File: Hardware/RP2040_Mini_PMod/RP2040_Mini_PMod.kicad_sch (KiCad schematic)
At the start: 37 parts, among them J3 Conn_02x06_Odd_Even, J4 USB_C_Receptacle_USB2.0, J5 Conn_01x04, SW1 SW_Push, SW2 SW_Push, U1 RP2040, U2 W25Q128JVS, U3 NCP1117-3.3_SOT223, Y1 12MHz

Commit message: continue with mini project
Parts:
- added J1: Micro_SD_Card, jjh:105162-0001, symbol Connector:Micro_SD_Card
- SW1, SW2: value SW_Push -> PTS815 SJK 250 SMTR LFS; footprint Button_Switch_THT:SW_PUSH_6mm_H4.3mm -> jjh:PTS815SJK250SMTRLFS
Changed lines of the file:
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@@
   (symbol (lib_id "Switch:SW_Push") (at 97.79 187.96 90) (unit 1)
     (in_bom yes) (on_board yes)
-    (property "Reference" "SW1" (id 0) (at 90.551 187.96 90))
-    (property "Value" "SW_Push" (id 1) (at 90.17 190.5 90))
-    (property "Footprint" "Button_Switch_THT:SW_PUSH_6mm_H4.3mm" (id 2) (at 92.71 187.96 0)
+    (property "Reference" "SW1" (id 0) (at 92.71 187.96 90))
+    (property "Value" "PTS815 SJK 250 SMTR LFS" (id 1) (at 87.63 180.34 0)
+      (effects (font (size 1.27 1.27)) hide)
+    )
+    (property "Footprint" "jjh:PTS815SJK250SMTRLFS" (id 2) (at 92.71 187.96 0)
       (effects (font (size 1.27 1.27)) hide)
     )
@@
   (symbol (lib_id "Switch:SW_Push") (at 144.78 182.88 90) (unit 1)
     (in_bom yes) (on_board yes)
-    (property "Reference" "SW2" (id 0) (at 137.541 182.88 0))
-    (property "Value" "SW_Push" (id 1) (at 139.8524 182.88 0))
-    (property "Footprint" "Button_Switch_THT:SW_PUSH_6mm_H4.3mm" (id 2) (at 139.7 182.88 0)
+    (property "Reference" "SW2" (id 0) (at 139.7 182.88 90))
+    (property "Value" "PTS815 SJK 250 SMTR LFS" (id 1) (at 139.8524 182.88 0)
+      (effects (font (size 1.27 1.27)) hide)
+    )
+    (property "Footprint" "jjh:PTS815SJK250SMTRLFS" (id 2) (at 139.7 182.88 0)
       (effects (font (size 1.27 1.27)) hide)
     )
@@
     (pin "1")
   )
+  (symbol (lib_id "Connector:Micro_SD_Card") (at 254 67.31 0) (unit 1)
+    (in_bom yes) (on_board yes) (fields_autoplaced)
+    (property "Reference" "J1" (id 0) (at 254.635 48.26 0))
+    (property "Value" "Micro_SD_Card" (id 1) (at 254.635 50.8 0))
+    (property "Footprint" "jjh:105162-0001" (id 2) (at 283.21 59.69 0)
+      (effects (font (size 1.27 1.27)) hide)
+    )
+    (property "Datasheet" "http://katalog.we-online.de/em/datasheet/693072010801.pdf" (id 3) (at 254 67.31 0)
+      (effects (font (size 1.27 1.27)) hide)
+    )
+    (pin "1")
+    (pin "2")
+    (pin "3")
+    (pin "4")
+    (pin "5")
+    (pin "6")
+    (pin "7")
+    (pin "8")
+    (pin "9")
+  )
   (symbol (lib_id "power:PWR_FLAG") (at 43.18 191.77 180) (unit 1)
     (in_bom yes) (on_board yes) (fields_autoplaced)
@@
       (reference "D3") (unit 1) (value "LED") (footprint "LED_SMD:LED_0603_1608Metric")
     )
+    (path "/e631d994-9bd2-4c7e-a12a-01901b43c7dc"
+      (reference "J1") (unit 1) (value "Micro_SD_Card") (footprint "jjh:105162-0001")
+    )
     (path "/00000000-0000-0000-0000-000060e95540"
       (reference "J3") (unit 1) (value "Conn_02x06_Odd_Even") (footprint "Connector_PinHeader_2.54mm:PinHeader_2x06_P2.54mm_Vertical")
@@
     )
     (path "/00000000-0000-0000-0000-000060ecf6f5"
-      (reference "SW1") (unit 1) (value "SW_Push") (footprint "Button_Switch_THT:SW_PUSH_6mm_H4.3mm")
+      (reference "SW1") (unit 1) (value "PTS815 SJK 250 SMTR LFS") (footprint "jjh:PTS815SJK250SMTRLFS")
     )
     (path "/00000000-0000-0000-0000-000060ed08d9"
-      (reference "SW2") (unit 1) (value "SW_Push") (footprint "Button_Switch_THT:SW_PUSH_6mm_H4.3mm")
+      (reference "SW2") (unit 1) (value "PTS815 SJK 250 SMTR LFS") (footprint "jjh:PTS815SJK250SMTRLFS")
     )
     (path "/00000000-0000-0000-0000-000060e8d0b0"

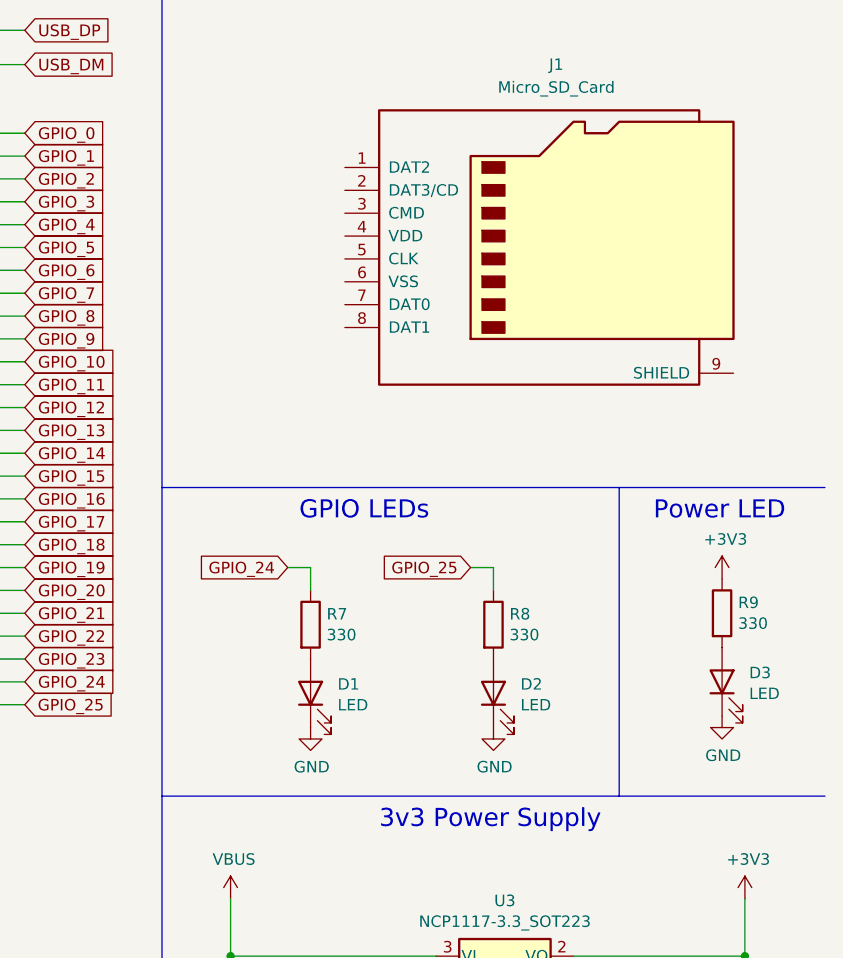
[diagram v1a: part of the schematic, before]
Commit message: Add the SD GPIO and RGB LED to schematic
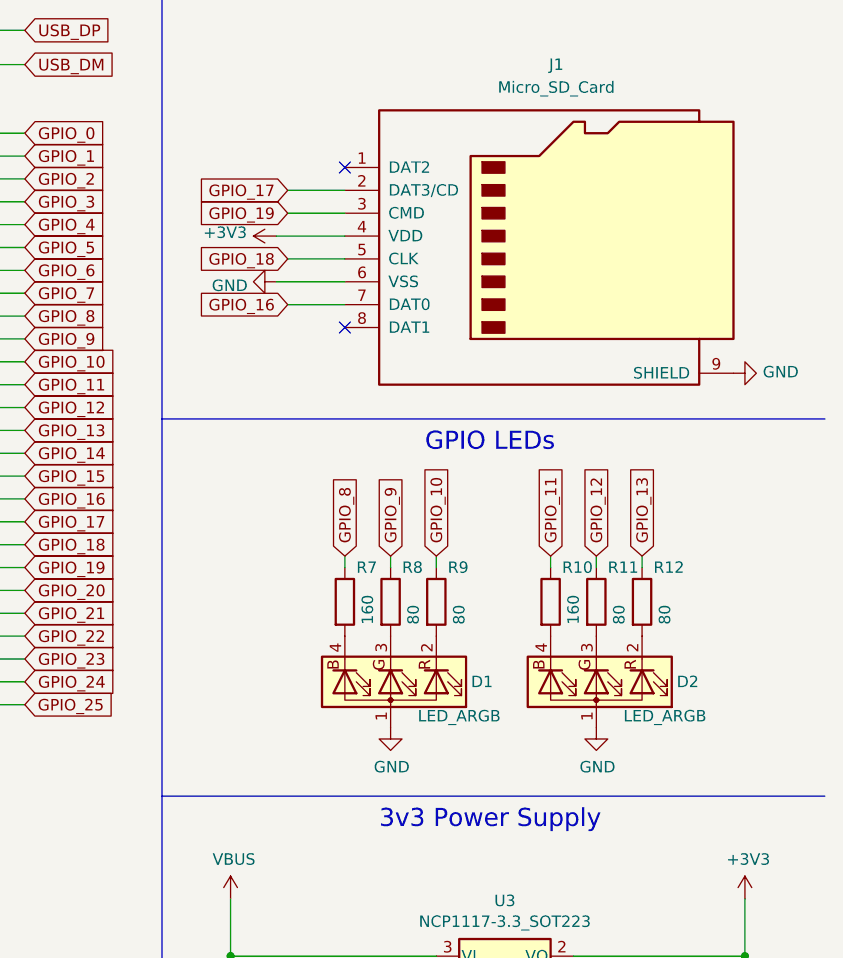
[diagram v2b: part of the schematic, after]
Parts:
- removed D1, D2, D3: LED, LED_SMD:LED_0603_1608Metric, symbol Device:LED
- added D1, D2: LED_ARGB, jjh:SX-0402-RGB, symbol Device:LED_ARGB
- added R10: 160, Resistor_SMD:R_0603_1608Metric, symbol Device:R
- added R11, R12: 80, Resistor_SMD:R_0603_1608Metric, symbol Device:R
- R7: value 330 -> 160
- R8, R9: value 330 -> 80
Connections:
- net +3V3: now also J1.4 (VDD); no longer R9.1
- net GND: now also J1.6 (VSS), J1.9 (SHIELD), D1.1 (A), D2.1 (A)
- net GPIO_10: now also R9.1
- net GPIO_11: now also R10.1
- net GPIO_12: now also R11.1
- net GPIO_13: now also R12.1
- net GPIO_16: now also J1.7 (DAT0)
- net GPIO_17: now also J1.2 (DAT3/CD)
- net GPIO_18: now also J1.5 (CLK)
- net GPIO_19: now also J1.3 (CMD)
- net GPIO_24: no longer R7.1
- net GPIO_25: no longer R8.1
- net GPIO_8: now also R7.1
- net GPIO_9: now also R8.1
- net at R7.2: now also D1.4 (BK)
- net at R8.2: now also D1.3 (GK)
- net at R9.2: now also D1.2 (RK)
- new net: D2.2 (RK), R12.2
- new net: D2.3 (GK), R11.2
- new net: D2.4 (BK), R10.2
- no-connect marks 6 -> 8
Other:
- note removed: "Power LED"

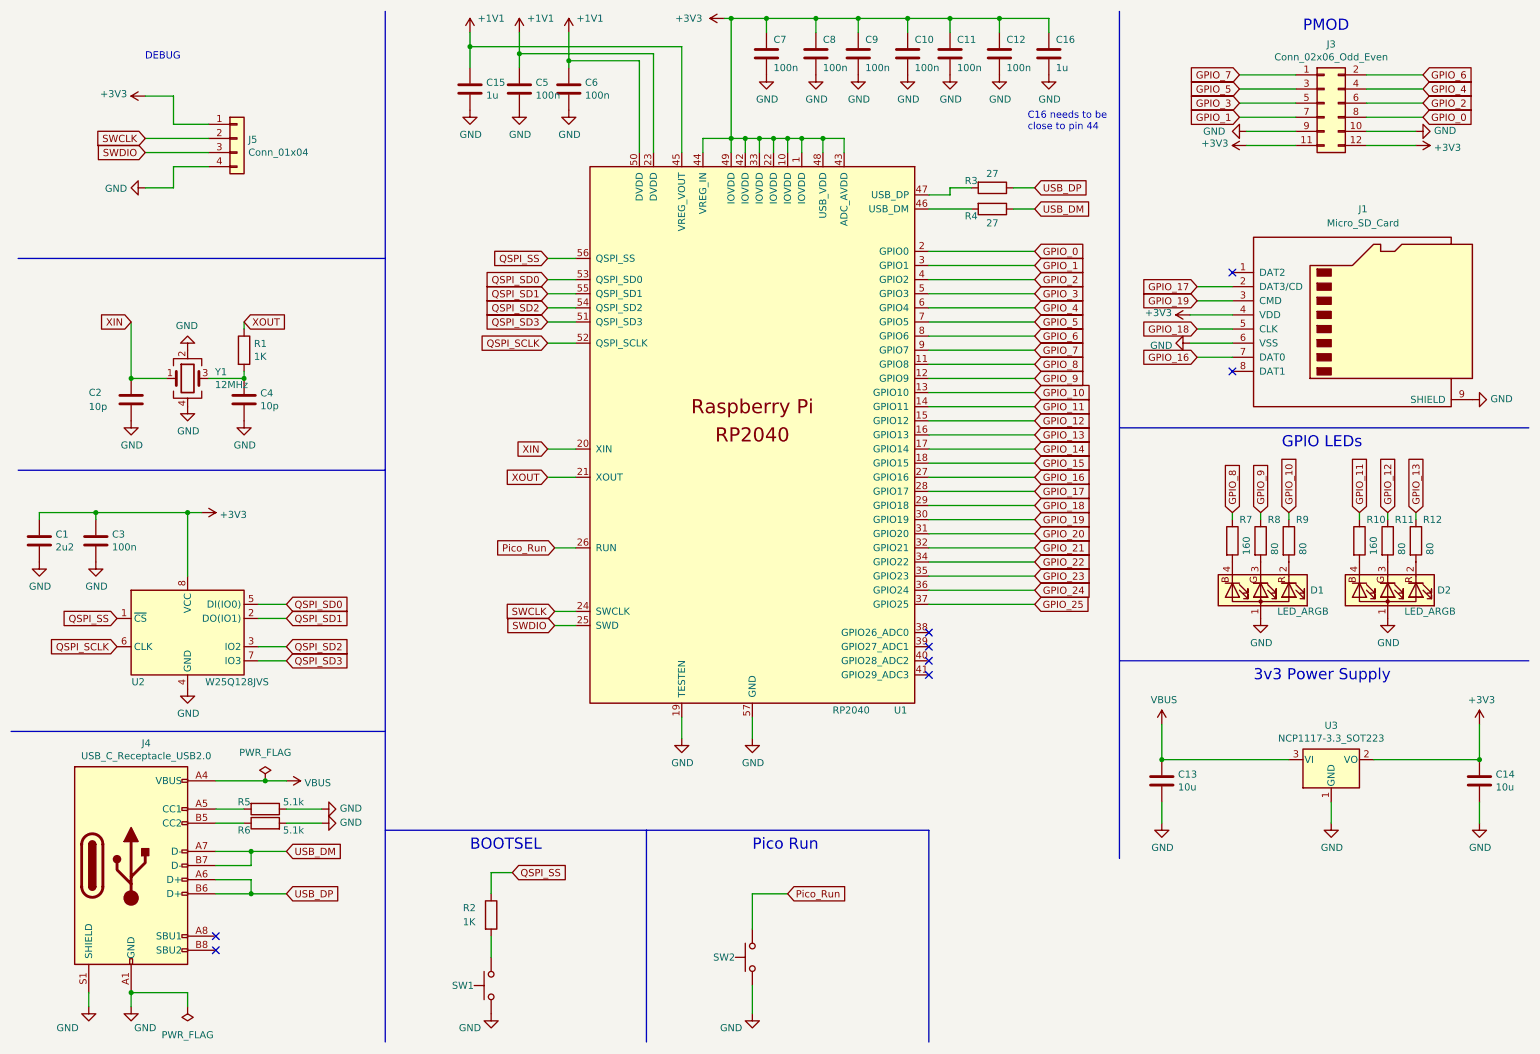
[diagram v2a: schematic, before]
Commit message: complete schematic and start pcb routing
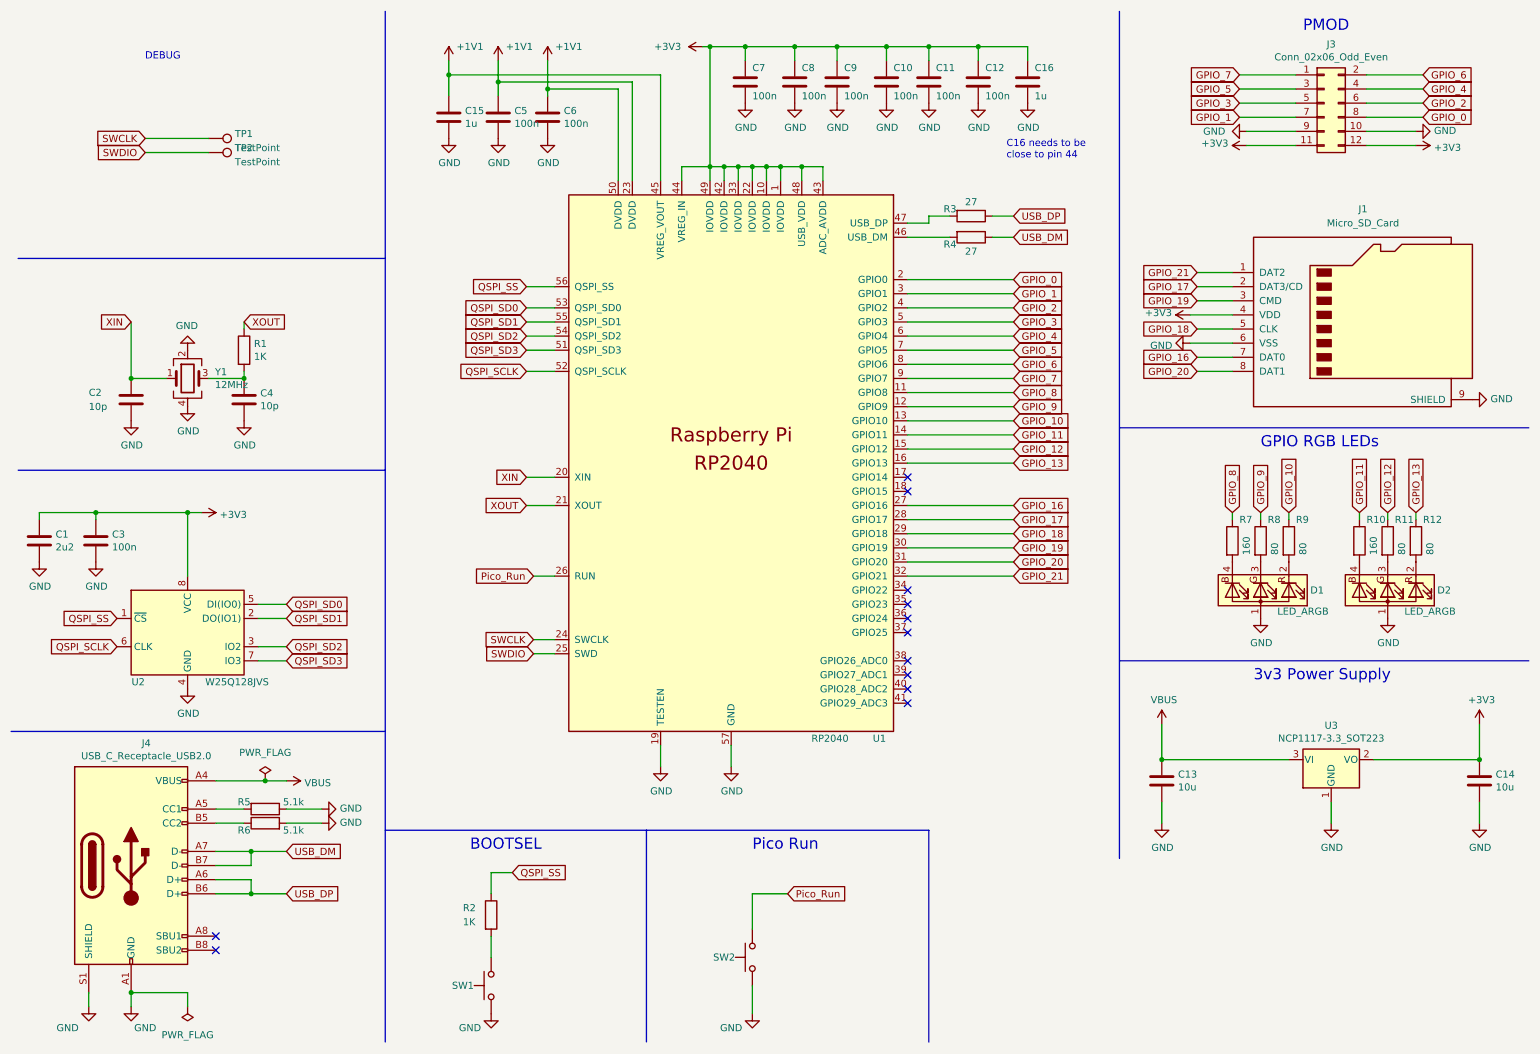
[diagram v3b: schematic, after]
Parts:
- removed J5: Conn_01x04, Connector_PinHeader_2.54mm:PinHeader_1x04_P2.54mm_Vertical, symbol Connector_Generic:Conn_01x04
- added TP1, TP2: TestPoint, TestPoint:TestPoint_Pad_D1.5mm, symbol Connector:TestPoint
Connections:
- net GPIO_20: now also J1.8 (DAT1)
- net GPIO_21: now also J1.1 (DAT2)
- net SWCLK: now also TP1.1
- net SWDIO: now also TP2.1
- net GPIO_14: no longer names the net of U1.17 (GPIO14)
- net GPIO_15: no longer names the net of U1.18 (GPIO15)
- net GPIO_22: no longer names the net of U1.34 (GPIO22)
- net GPIO_23: no longer names the net of U1.35 (GPIO23)
- net GPIO_24: no longer names the net of U1.36 (GPIO24)
- net GPIO_25: no longer names the net of U1.37 (GPIO25)
- no-connect marks 8 -> 12
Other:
- note added: "GPIO RGB LEDs"
- note removed: "GPIO LEDs"
- title: PMOD for Raspberry Pi RP2040 -> Mini PMOD RP2040
- moved on the sheet: C10, C11, C12, C15, C16, C5, C6, C7, C8, C9, R3, R4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

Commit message: update switch layout and sd card gnd pins
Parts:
- removed SW1, SW2: PTS815 SJK 250 SMTR LFS, jjh:PTS815SJK250SMTRLFS, symbol Switch:SW_Push
- added SW1, SW2: PTS815 SJK 250 SMTR LFS, jjh:PTS815SJK250SMTRLFS, symbol Switch:SW_MEC_5E
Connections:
- net GND: now also SW1.1, SW2.1
- net Pico_Run: now also SW1.4 (A)
- net at R2.2: now also SW2.4 (A)
- no-connect marks 12 -> 16
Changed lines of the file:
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@@
   (no_connect (at 172.72 124.46))
   (no_connect (at 172.72 137.16))
+  (no_connect (at 100.33 182.88))
   (no_connect (at 172.72 116.84))
   (no_connect (at 172.72 96.52))
+  (no_connect (at 147.32 187.96))
   (no_connect (at 172.72 134.62))
   (no_connect (at 48.26 179.07))
   (no_connect (at 172.72 121.92))
+  (no_connect (at 147.32 177.8))
   (no_connect (at 48.26 181.61))
+  (no_connect (at 100.33 193.04))
   (no_connect (at 172.72 99.06))
   (no_connect (at 172.72 119.38))
@@
     (pin "1")
   )
-  (symbol (lib_id "Switch:SW_Push") (at 97.79 187.96 90) (unit 1)
-    (in_bom yes) (on_board yes)
-    (property "Reference" "SW1" (id 0) (at 92.71 187.96 90))
-    (property "Value" "PTS815 SJK 250 SMTR LFS" (id 1) (at 87.63 180.34 0)
-      (effects (font (size 1.27 1.27)) hide)
-    )
-    (property "Footprint" "jjh:PTS815SJK250SMTRLFS" (id 2) (at 92.71 187.96 0)
-      (effects (font (size 1.27 1.27)) hide)
-    )
-    (property "Datasheet" "~" (id 3) (at 92.71 187.96 0)
-      (effects (font (size 1.27 1.27)) hide)
-    )
-    (pin "1")
-    (pin "2")
-  )
-  (symbol (lib_id "Switch:SW_Push") (at 144.78 182.88 90) (unit 1)
-    (in_bom yes) (on_board yes)
-    (property "Reference" "SW2" (id 0) (at 139.7 182.88 90))
-    (property "Value" "PTS815 SJK 250 SMTR LFS" (id 1) (at 139.8524 182.88 0)
-      (effects (font (size 1.27 1.27)) hide)
-    )
-    (property "Footprint" "jjh:PTS815SJK250SMTRLFS" (id 2) (at 139.7 182.88 0)
-      (effects (font (size 1.27 1.27)) hide)
-    )
-    (property "Datasheet" "~" (id 3) (at 139.7 182.88 0)
-      (effects (font (size 1.27 1.27)) hide)
-    )
-    (pin "1")
-    (pin "2")
-  )
   (symbol (lib_id "power:GND") (at 97.79 193.04 0) (unit 1)
     (in_bom yes) (on_board yes)
@@
     (pin "1")
   )
+  (symbol (lib_id "Switch:SW_MEC_5E") (at 100.33 187.96 90) (unit 1)
+    (in_bom yes) (on_board yes) (fields_autoplaced)
+    (property "Reference" "SW2" (id 0) (at 100.965 188.3938 90)
+      (effects (font (size 1.27 1.27)) (justify right))
+    )
+    (property "Value" "PTS815 SJK 250 SMTR LFS" (id 1) (at 93.7061 187.96 0)
+      (effects (font (size 1.27 1.27)) hide)
+    )
+    (property "Footprint" "jjh:PTS815SJK250SMTRLFS" (id 2) (at 92.71 187.96 0)
+      (effects (font (size 1.27 1.27)) hide)
+    )
+    (property "Datasheet" "http://www.apem.com/int/index.php?controller=attachment&id_attachment=1371" (id 3) (at 92.71 187.96 0)
+      (effects (font (size 1.27 1.27)) hide)
+    )
+    (pin "1")
+    (pin "2")
+    (pin "3")
+    (pin "4")
+  )
   (symbol (lib_id "Device:R") (at 264.16 107.95 0) (unit 1)
     (in_bom yes) (on_board yes)
@@
     )
     (pin "1")
+  )
+  (symbol (lib_id "Switch:SW_MEC_5E") (at 147.32 182.88 90) (unit 1)
+    (in_bom yes) (on_board yes) (fields_autoplaced)
+    (property "Reference" "SW1" (id 0) (at 147.955 183.3138 90)
+      (effects (font (size 1.27 1.27)) (justify right))
+    )
+    (property "Value" "PTS815 SJK 250 SMTR LFS" (id 1) (at 140.6961 182.88 0)
+      (effects (font (size 1.27 1.27)) hide)
+    )
+    (property "Footprint" "jjh:PTS815SJK250SMTRLFS" (id 2) (at 139.7 182.88 0)
+      (effects (font (size 1.27 1.27)) hide)
+    )
+    (property "Datasheet" "http://www.apem.com/int/index.php?controller=attachment&id_attachment=1371" (id 3) (at 139.7 182.88 0)
+      (effects (font (size 1.27 1.27)) hide)
+    )
+    (pin "1")
+    (pin "2")
+    (pin "3")
+    (pin "4")
   )
   (symbol (lib_id "power:+3V3") (at 223.52 67.31 90) (unit 1)
@@
       (reference "R12") (unit 1) (value "80") (footprint "Resistor_SMD:R_0603_1608Metric")
     )
-    (path "/00000000-0000-0000-0000-000060ecf6f5"
+    (path "/95d1ffd3-518e-4859-a770-5ef5964ebf37"
       (reference "SW1") (unit 1) (value "PTS815 SJK 250 SMTR LFS") (footprint "jjh:PTS815SJK250SMTRLFS")
     )
-    (path "/00000000-0000-0000-0000-000060ed08d9"
+    (path "/8b278666-5d04-4b15-8425-4128144fb860"
       (reference "SW2") (unit 1) (value "PTS815 SJK 250 SMTR LFS") (footprint "jjh:PTS815SJK250SMTRLFS")
     )

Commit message: remove usb sheild from usb connector
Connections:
- net GND: no longer J4.S1 (SHIELD)
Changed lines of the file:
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@@
-    (stroke (width 0) (type default) (color 0 0 0 0))
-  )
-  (wire (pts (xy 25.4 191.77) (xy 25.4 189.23))
     (stroke (width 0) (type default) (color 0 0 0 0))
   )
@@
     (pin "B8")
     (pin "B9")
-    (pin "S1")
   )
   (symbol (lib_id "Memory_Flash:W25Q128JVS") (at 43.18 124.46 0) (unit 1)
@@
     )
     (property "Datasheet" "" (id 3) (at 33.02 191.77 0)
-      (effects (font (size 1.27 1.27)) hide)
-    )
-    (pin "1")
-  )
-  (symbol (lib_id "power:GND") (at 25.4 191.77 0) (unit 1)
-    (in_bom yes) (on_board yes)
-    (property "Reference" "#PWR0117" (id 0) (at 25.4 198.12 0)
-      (effects (font (size 1.27 1.27)) hide)
-    )
-    (property "Value" "GND" (id 1) (at 21.59 195.58 0))
-    (property "Footprint" "" (id 2) (at 25.4 191.77 0)
-      (effects (font (size 1.27 1.27)) hide)
-    )
-    (property "Datasheet" "" (id 3) (at 25.4 191.77 0)
       (effects (font (size 1.27 1.27)) hide)
     )
@@
       (reference "#PWR0116") (unit 1) (value "GND") (footprint "")
     )
-    (path "/00000000-0000-0000-0000-000060f0dfc6"
-      (reference "#PWR0117") (unit 1) (value "GND") (footprint "")
-    )
     (path "/00000000-0000-0000-0000-000060f4fcce"
